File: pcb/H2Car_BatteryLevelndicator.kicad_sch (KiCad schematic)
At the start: 14 parts, among them J1 Conn_01x01_Pin, J2 Conn_01x02, J3 Conn_01x01_Pin, U1 XIAO-nRF52840-SMD, U3 MIC5219-3.3YM5

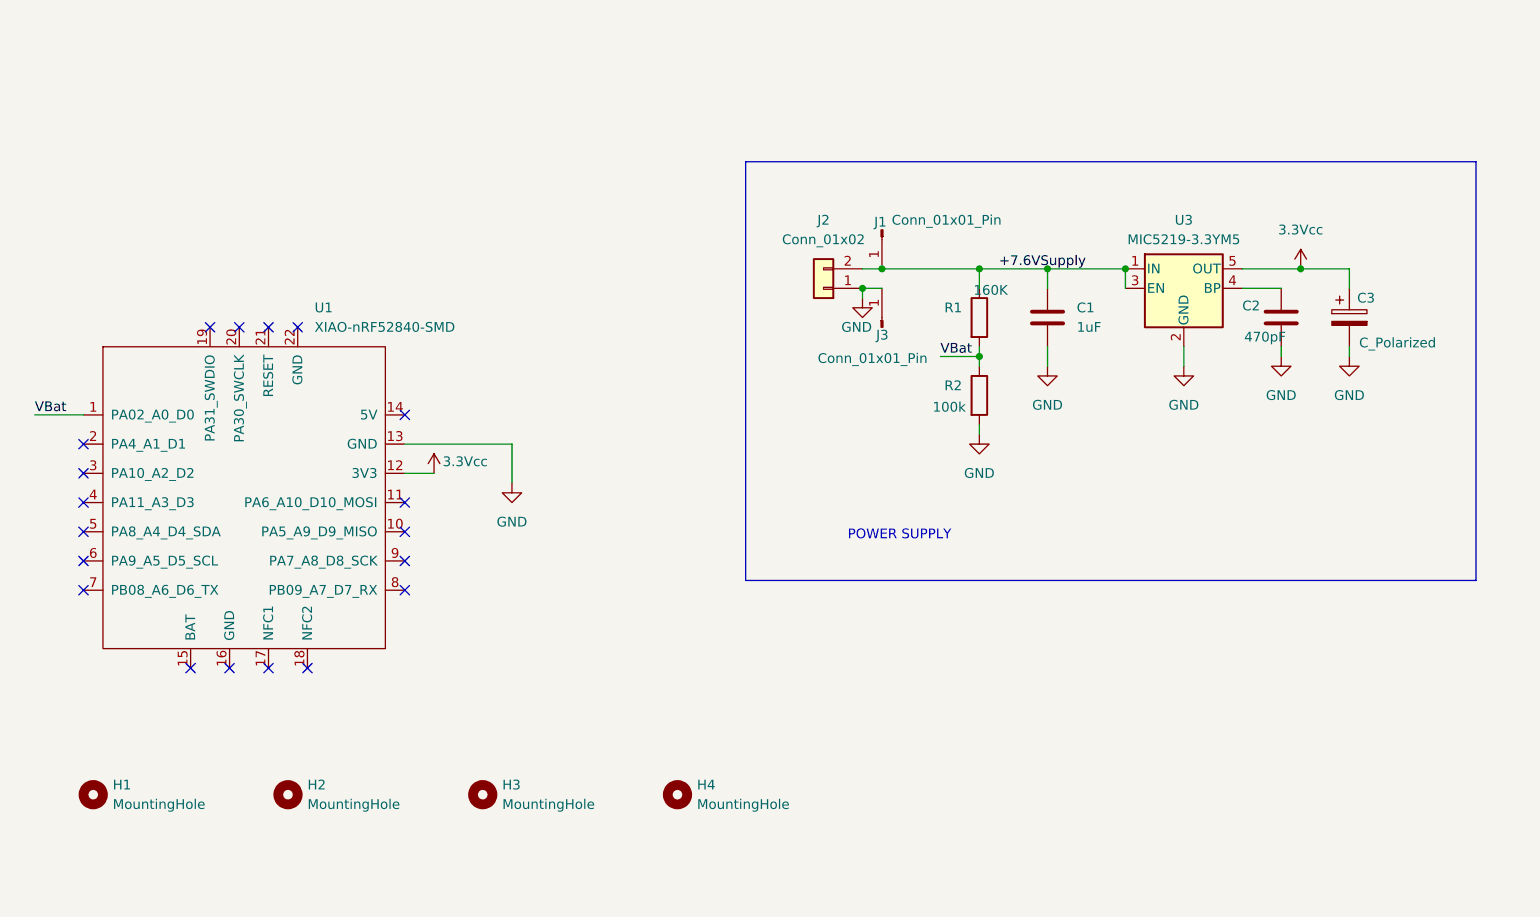
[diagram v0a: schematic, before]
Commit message: Include battery parameters in readme. Make schematic design more readable.
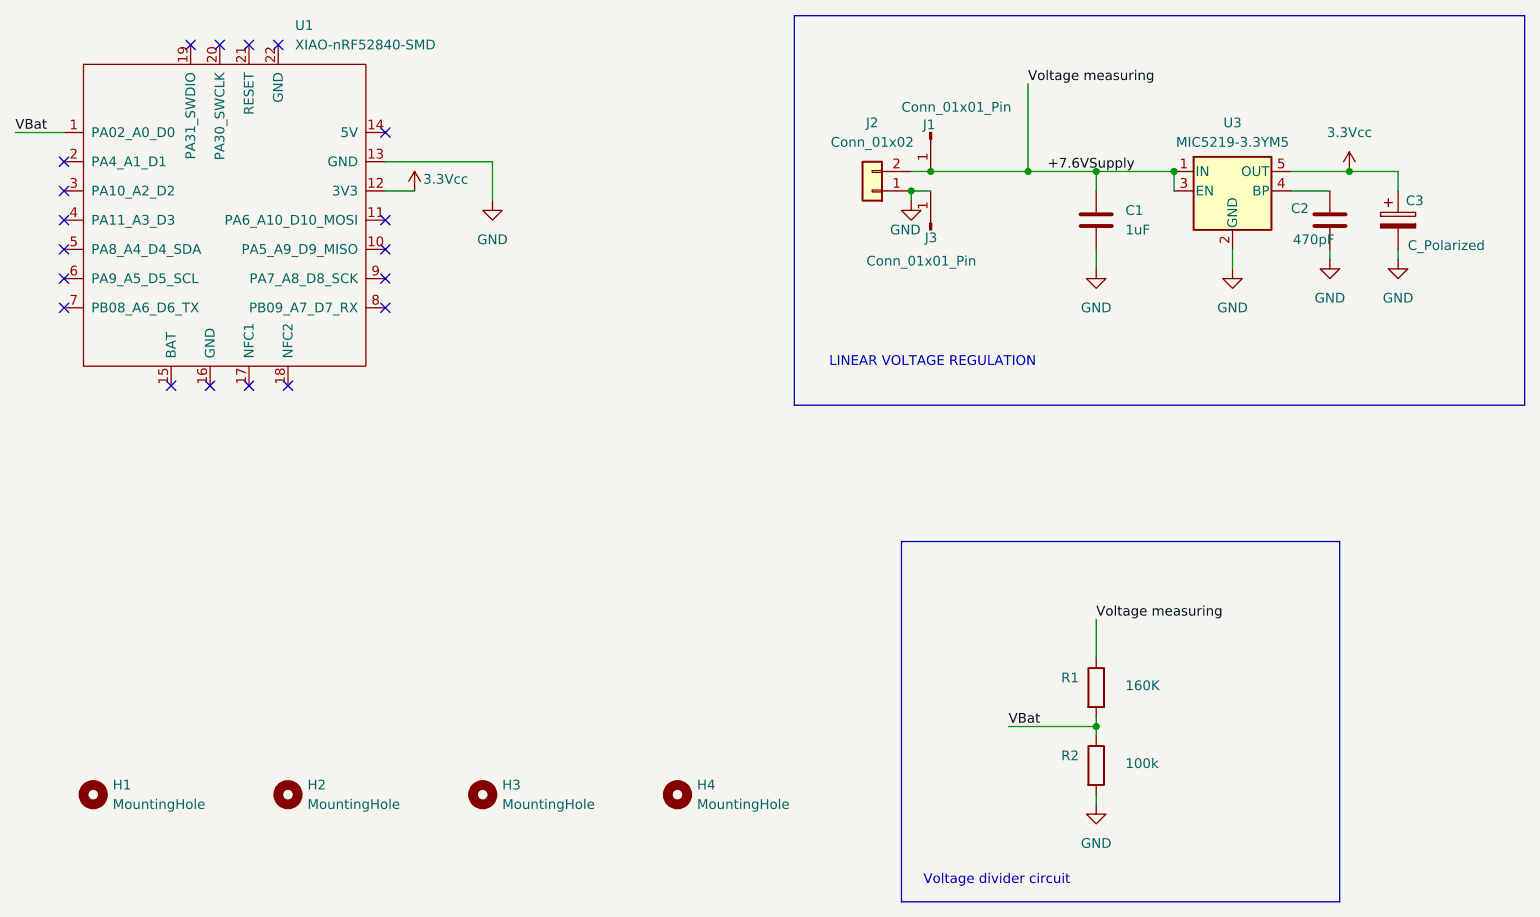
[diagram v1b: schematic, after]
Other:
- note added: "LINEAR VOLTAGE REGULATION"
- note added: "Voltage divider circuit"
- note removed: "POWER SUPPLY"
- moved on the sheet: C1, C2, C3, J1, J2, J3, U1, U3
